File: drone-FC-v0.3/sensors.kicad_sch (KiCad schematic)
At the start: 14 parts, among them J2 Conn_01x04_Pin, U3 BMI088, U6 LIS3MDL, U7 MS5607-02BA

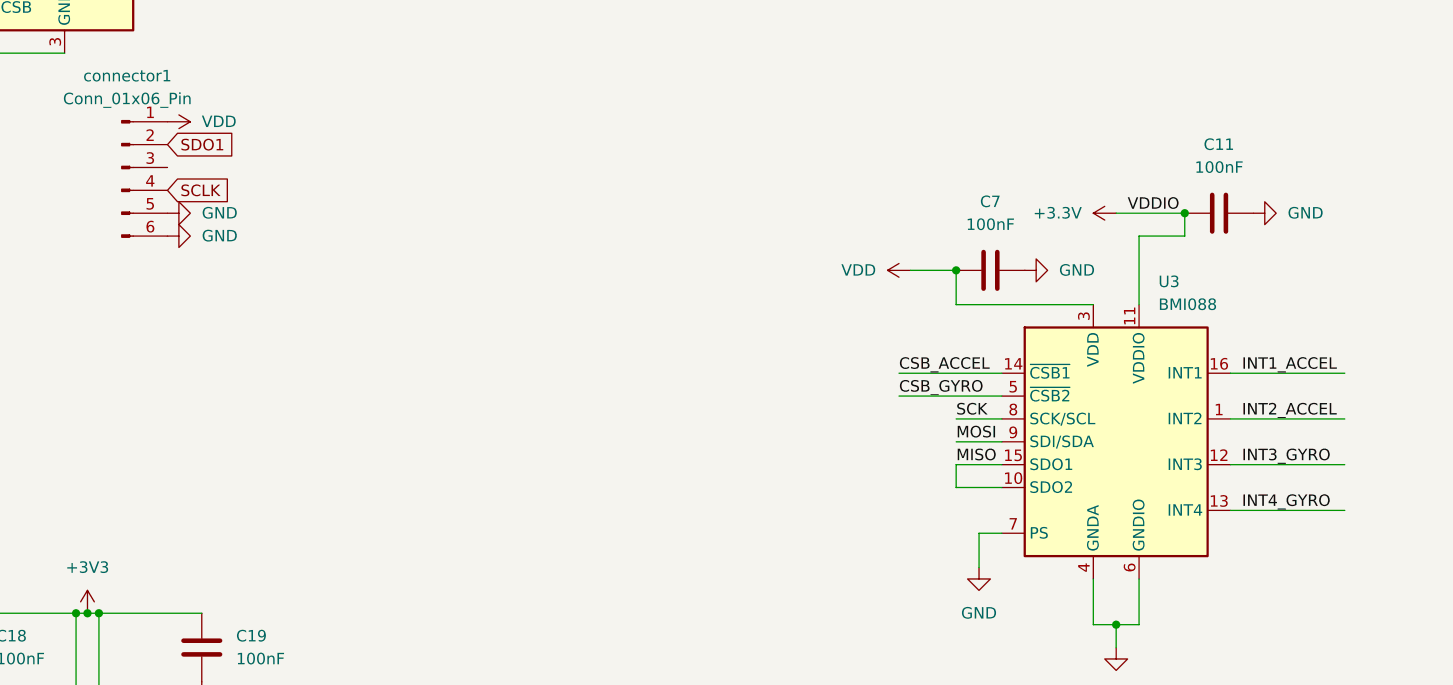
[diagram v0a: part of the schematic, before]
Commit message: added global labels for BMI088
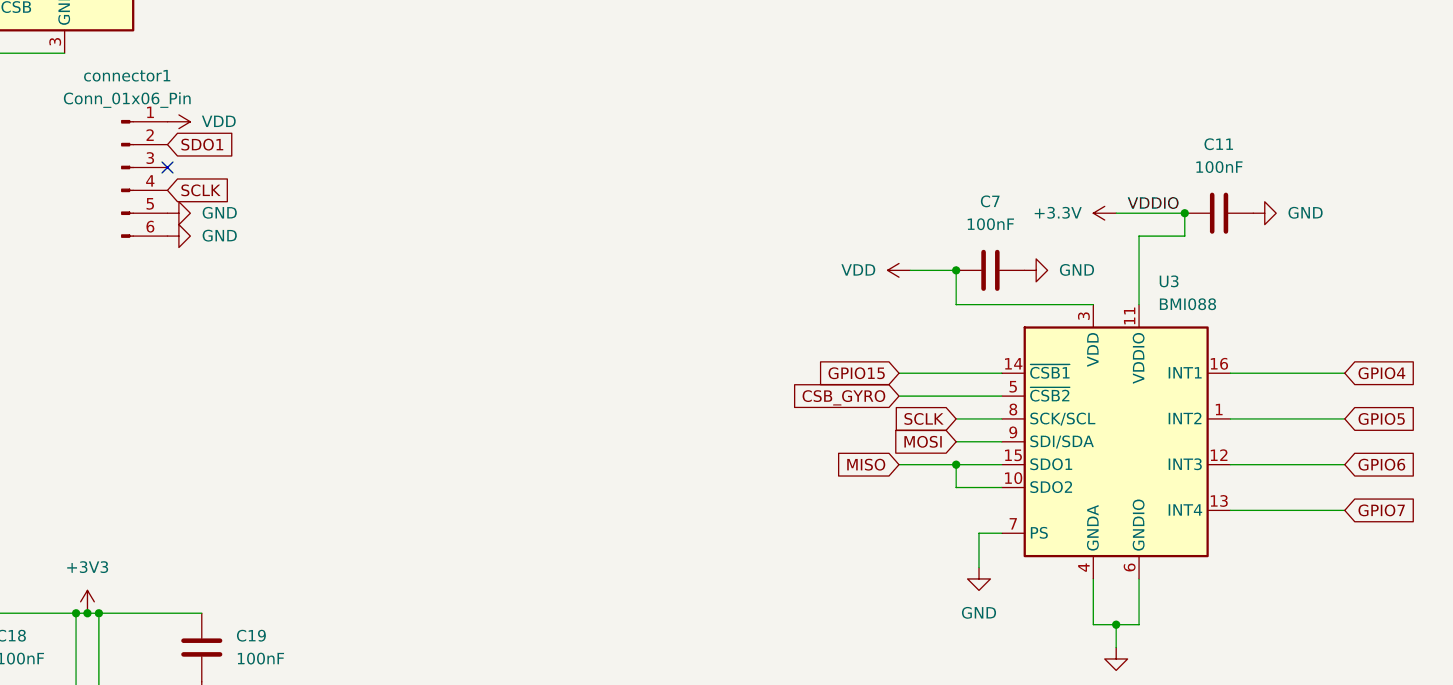
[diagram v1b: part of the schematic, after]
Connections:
- net SCK is gone; now on net SCLK: U3.8 (SCK/SCL)
- net CSB_ACCEL renamed GPIO15
- net INT1_ACCEL renamed GPIO4
- net INT2_ACCEL renamed GPIO5
- net INT3_GYRO renamed GPIO6
- net INT4_GYRO renamed GPIO7
- no-connect marks 4 -> 5

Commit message: added sda and scl labels
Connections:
- net SDA_MAG is gone; now on net SDA: J2.3 (Pin_3), R8.2, U6.11 (SDA/SDI/SDO)
- net SDO1 is gone; now on net SDA: connector1.2 (Pin_2)
- net SCLK: no longer R10.2, U7.8 (SCLK), connector1.4 (Pin_4)
- net GPIO 8 renamed SDA
- net SCL_MAG renamed SCL
- net SCL: now also R10.2, U7.8 (SCLK), connector1.4 (Pin_4)

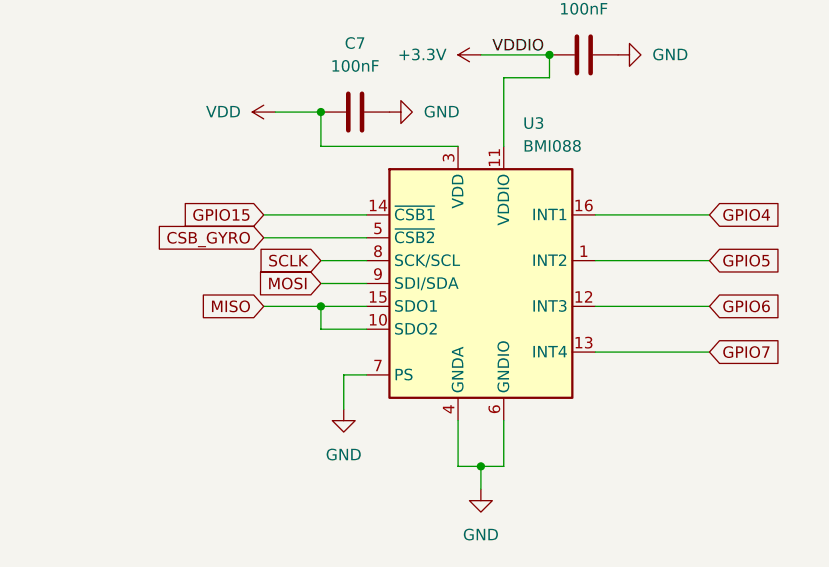
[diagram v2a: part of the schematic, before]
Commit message: added connections and ground plane
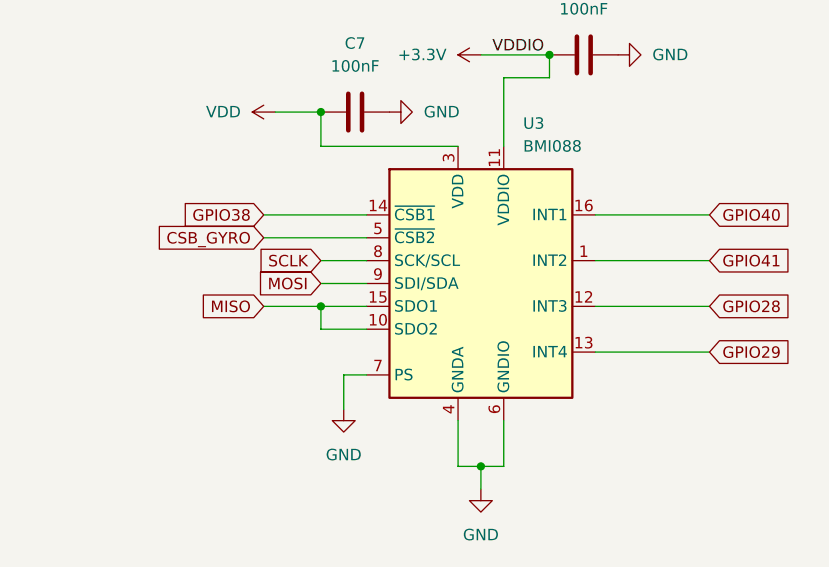
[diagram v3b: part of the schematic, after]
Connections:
- net GPIO15 renamed GPIO38
- net GPIO4 renamed GPIO40
- net GPIO5 renamed GPIO41
- net GPIO6 renamed GPIO28
- net GPIO7 renamed GPIO29
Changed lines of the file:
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@@
 		)
 	)
-	(global_label "GPIO4"
+	(global_label "GPIO40"
 		(shape input)
 		(at 232.41 97.79 0)
@@
 		)
 		(property "Intersheetrefs" "${INTERSHEET_REFS}"
-			(at 241.08 97.79 0)
-			(hide yes)
-			(show_name no)
-			(do_not_autoplace no)
-			(effects
-				(font
-					(size 1.27 1.27)
-				)
-				(justify left)
-			)
-		)
-	)
-	(global_label "GPIO7"
+			(at 242.2895 97.79 0)
+			(hide yes)
+			(show_name no)
+			(do_not_autoplace no)
+			(effects
+				(font
+					(size 1.27 1.27)
+				)
+				(justify left)
+			)
+		)
+	)
+	(global_label "GPIO29"
 		(shape input)
 		(at 232.41 113.03 0)
@@
 		)
 		(property "Intersheetrefs" "${INTERSHEET_REFS}"
-			(at 241.08 113.03 0)
+			(at 242.2895 113.03 0)
 			(hide yes)
 			(show_name no)
@@
 		)
 	)
-	(global_label "GPIO5"
+	(global_label "GPIO41"
 		(shape input)
 		(at 232.41 102.87 0)
@@
 		)
 		(property "Intersheetrefs" "${INTERSHEET_REFS}"
-			(at 241.08 102.87 0)
-			(hide yes)
-			(show_name no)
-			(do_not_autoplace no)
-			(effects
-				(font
-					(size 1.27 1.27)
-				)
-				(justify left)
-			)
-		)
-	)
-	(global_label "GPIO15"
+			(at 242.2895 102.87 0)
+			(hide yes)
+			(show_name no)
+			(do_not_autoplace no)
+			(effects
+				(font
+					(size 1.27 1.27)
+				)
+				(justify left)
+			)
+		)
+	)
+	(global_label "GPIO38"
 		(shape input)
 		(at 182.88 97.79 180)
@@
 		)
 	)
-	(global_label "GPIO6"
+	(global_label "GPIO28"
 		(shape input)
 		(at 232.41 107.95 0)
@@
 		)
 		(property "Intersheetrefs" "${INTERSHEET_REFS}"
-			(at 241.08 107.95 0)
-			(hide yes)
-			(show_name no)
+			(at 242.2895 107.95 0)
+			(hide yes)
+			(show_name no)
